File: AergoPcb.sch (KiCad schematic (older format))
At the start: 16 parts

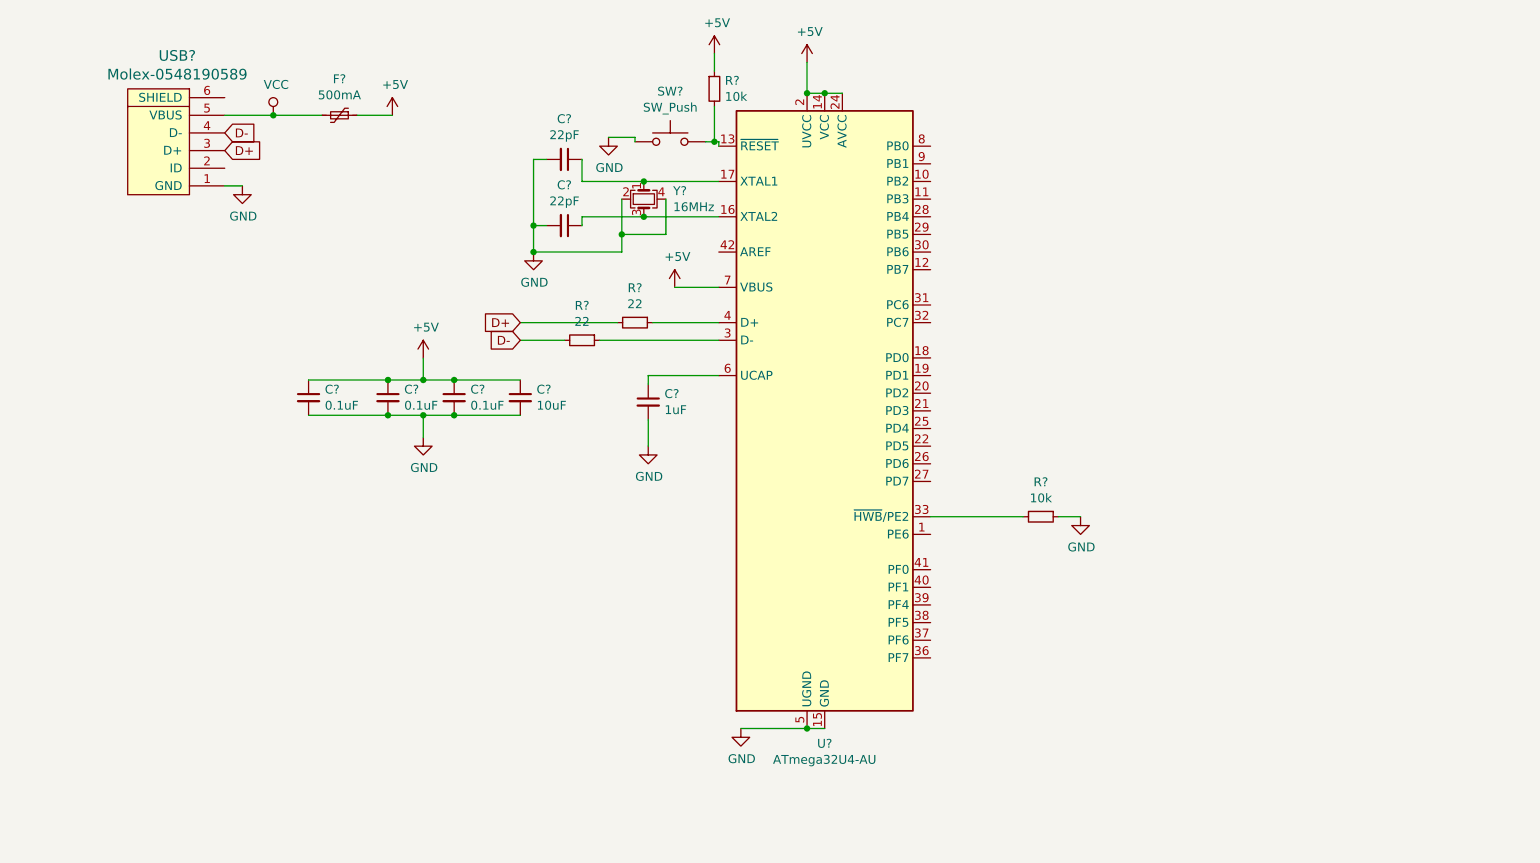
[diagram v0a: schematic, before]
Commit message: more work, added rgb strip and backlighting
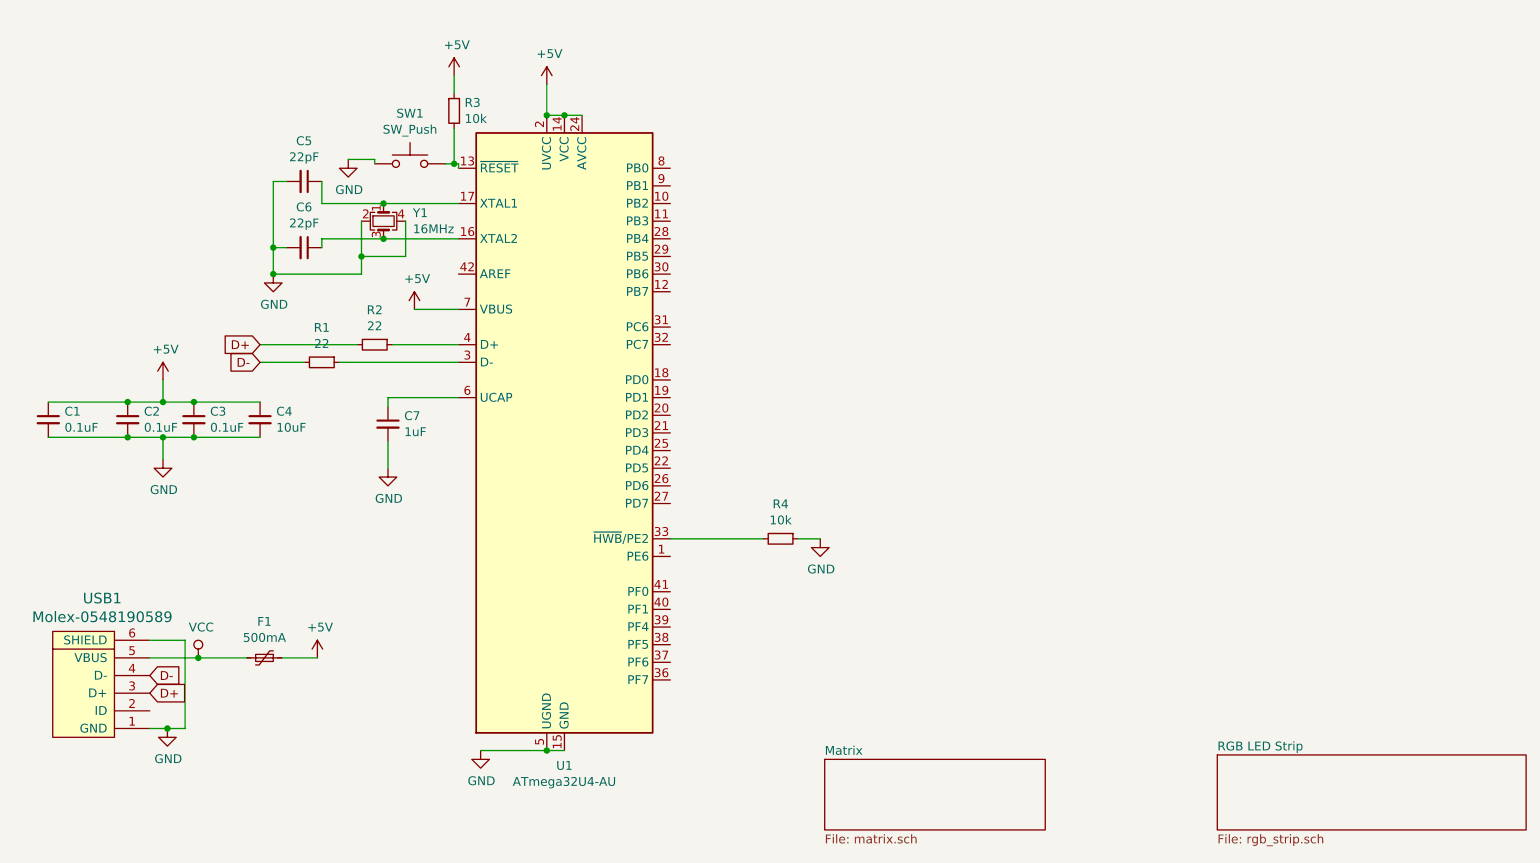
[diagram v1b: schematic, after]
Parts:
- gave numbers to parts that had none: 16
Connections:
- net GND: now also USB1.6 (SHIELD)
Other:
- moved on the sheet: C1, C2, C3, C4, C5, C6, C7, F1, R1, R2, R3, R4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
